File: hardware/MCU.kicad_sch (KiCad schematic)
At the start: 34 parts, among them J2 USB_C_Receptacle_USB2.0_16P, J3 Sensor, J4 Display, Q2 MMBT3904, Q3 MMBT3904, U2 CP2102-GM, U3 AKS1201, U4 ESP32-WROOM-32E-N4

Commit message: updated layout
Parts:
- added C22: 1u, Capacitor_SMD:C_0603_1608Metric, symbol Device:C_Small
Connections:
- net 3V3_MCU: now also C22.1
- net GND: now also C22.2
- net USB_CONN_D+: now reaches J2.A7 (D-), J2.B7 (D-), U3.1 (I/O1)
- net USB_CONN_D-: now reaches J2.A6 (D+), J2.B6 (D+), U3.3 (I/O2)
- net USB_DM renamed USB_D+
- net USB_D+: now also U2.4 (D+); no longer U2.5 (D-)
- net USB_DP renamed USB_D-
- net USB_D-: now also U2.5 (D-); no longer U2.4 (D+)
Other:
- moved on the sheet: R10, R11, R17, U3

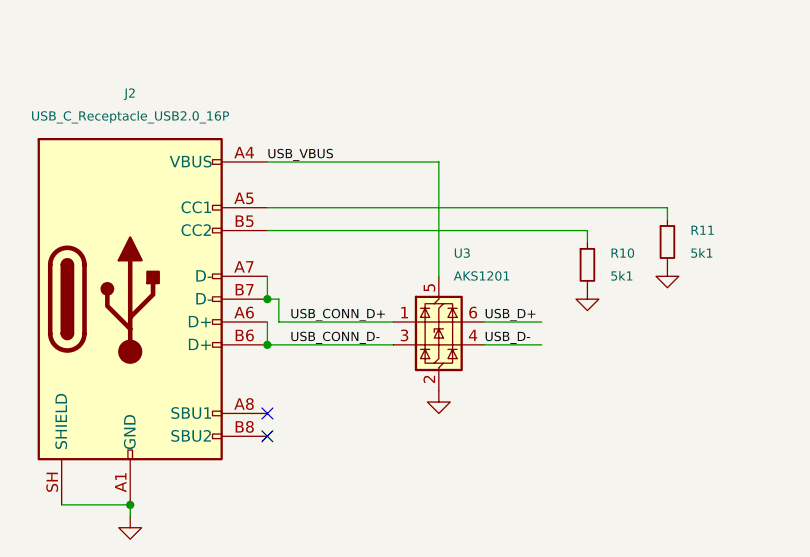
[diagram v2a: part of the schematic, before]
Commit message: updated layout
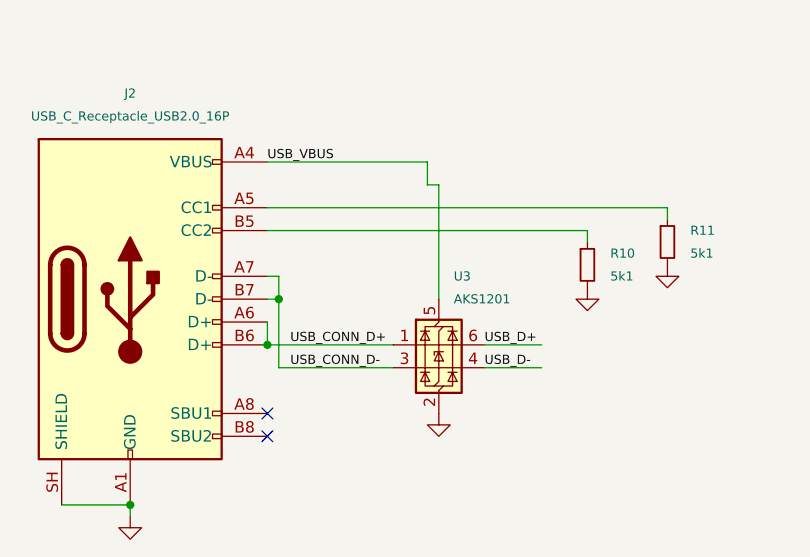
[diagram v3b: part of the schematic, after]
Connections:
- net USB_CONN_D+: now also J2.A6 (D+), J2.B6 (D+); no longer J2.A7 (D-), J2.B7 (D-)
- net USB_CONN_D-: now also J2.A7 (D-), J2.B7 (D-); no longer J2.A6 (D+), J2.B6 (D+)
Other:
- moved on the sheet: U3
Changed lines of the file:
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@@
 	)
 	(junction
+		(at 91.44 163.83)
+		(diameter 0)
+		(color 0 0 0 0)
+	)
+	(junction
 		(at 143.51 62.23)
 		(diameter 0)
@@
 	)
 	(junction
-		(at 90.17 168.91)
-		(diameter 0)
-		(color 0 0 0 0)
-	)
-	(junction
 		(at 228.6 100.33)
 		(diameter 0)
@@
 	)
 	(junction
-		(at 90.17 163.83)
+		(at 90.17 168.91)
 		(diameter 0)
 		(color 0 0 0 0)
@@
 	(wire
 		(pts
+			(xy 107.95 148.59) (xy 90.17 148.59)
+		)
+		(stroke
+			(width 0)
+			(type default)
+		)
+	)
+	(wire
+		(pts
 			(xy 90.17 45.72) (xy 90.17 46.99)
 		)
@@
 	(wire
 		(pts
-			(xy 114.3 168.91) (xy 120.65 168.91)
+			(xy 114.3 171.45) (xy 120.65 171.45)
 		)
 		(stroke
@@
 	(wire
 		(pts
-			(xy 109.22 161.29) (xy 109.22 148.59)
+			(xy 109.22 163.83) (xy 109.22 151.13)
 		)
 		(stroke
@@
 	(wire
 		(pts
-			(xy 90.17 161.29) (xy 90.17 163.83)
+			(xy 90.17 168.91) (xy 104.14 168.91)
 		)
 		(stroke
@@
 	(wire
 		(pts
-			(xy 91.44 163.83) (xy 90.17 163.83)
-		)
-		(stroke
-			(width 0)
-			(type default)
-		)
-	)
-	(wire
-		(pts
 			(xy 90.17 52.07) (xy 90.17 53.34)
 		)
@@
 	(wire
 		(pts
+			(xy 90.17 163.83) (xy 91.44 163.83)
+		)
+		(stroke
+			(width 0)
+			(type default)
+		)
+	)
+	(wire
+		(pts
 			(xy 251.46 96.52) (xy 251.46 97.79)
 		)
@@
 	(wire
 		(pts
+			(xy 91.44 171.45) (xy 104.14 171.45)
+		)
+		(stroke
+			(width 0)
+			(type default)
+		)
+	)
+	(wire
+		(pts
 			(xy 199.39 115.57) (xy 201.93 115.57)
 		)
@@
 	(wire
 		(pts
-			(xy 165.1 41.91) (xy 184.15 41.91)
+			(xy 90.17 161.29) (xy 91.44 161.29)
 		)
 		(stroke
@@
 	(wire
 		(pts
-			(xy 66.04 45.72) (xy 73.66 45.72)
+			(xy 165.1 41.91) (xy 184.15 41.91)
 		)
 		(stroke
@@
 	(wire
 		(pts
-			(xy 91.44 163.83) (xy 91.44 166.37)
+			(xy 66.04 45.72) (xy 73.66 45.72)
 		)
 		(stroke
@@
 	(wire
 		(pts
-			(xy 90.17 166.37) (xy 90.17 168.91)
+			(xy 80.01 45.72) (xy 80.01 46.99)
 		)
 		(stroke
@@
 	(wire
 		(pts
-			(xy 80.01 45.72) (xy 80.01 46.99)
+			(xy 205.74 49.53) (xy 205.74 41.91)
 		)
 		(stroke
@@
 	(wire
 		(pts
-			(xy 205.74 49.53) (xy 205.74 41.91)
+			(xy 248.92 114.3) (xy 248.92 102.87)
 		)
 		(stroke
@@
 	(wire
 		(pts
-			(xy 248.92 114.3) (xy 248.92 102.87)
+			(xy 217.17 102.87) (xy 238.76 102.87)
 		)
 		(stroke
@@
 	(wire
 		(pts
-			(xy 217.17 102.87) (xy 238.76 102.87)
+			(xy 91.44 161.29) (xy 91.44 163.83)
 		)
 		(stroke
@@
 	(wire
 		(pts
+			(xy 107.95 151.13) (xy 107.95 148.59)
+		)
+		(stroke
+			(width 0)
+			(type default)
+		)
+	)
+	(wire
+		(pts
 			(xy 175.26 48.26) (xy 175.26 49.53)
 		)
@@
 	(wire
 		(pts
-			(xy 90.17 148.59) (xy 109.22 148.59)
+			(xy 107.95 151.13) (xy 109.22 151.13)
 		)
 		(stroke
@@
 	(wire
 		(pts
-			(xy 114.3 166.37) (xy 120.65 166.37)
+			(xy 114.3 168.91) (xy 120.65 168.91)
 		)
 		(stroke
@@
 	(wire
 		(pts
-			(xy 91.44 166.37) (xy 104.14 166.37)
+			(xy 228.6 86.36) (xy 228.6 88.9)
 		)
 		(stroke
@@
 	(wire
 		(pts
-			(xy 228.6 86.36) (xy 228.6 88.9)
+			(xy 175.26 41.91) (xy 175.26 43.18)
 		)
 		(stroke
@@
 	(wire
 		(pts
-			(xy 175.26 41.91) (xy 175.26 43.18)
+			(xy 90.17 166.37) (xy 90.17 168.91)
 		)
 		(stroke
@@
 	(wire
 		(pts
+			(xy 91.44 163.83) (xy 91.44 171.45)
+		)
+		(stroke
+			(width 0)
+			(type default)
+		)
+	)
+	(wire
+		(pts
 			(xy 154.94 48.26) (xy 154.94 49.53)
 		)
@@
 	(wire
 		(pts
-			(xy 90.17 168.91) (xy 104.14 168.91)
-		)
-		(stroke
-			(width 0)
-			(type default)
-		)
-	)
-	(wire
-		(pts
 			(xy 199.39 100.33) (xy 228.6 100.33)
 		)
@@
 	)
 	(label "USB_CONN_D+"
-		(at 92.71 166.37 0)
+		(at 92.71 168.91 0)
 		(effects
 			(font
@@
 	)
 	(label "USB_D+"
-		(at 114.3 166.37 0)
+		(at 114.3 168.91 0)
 		(effects
 			(font
@@
 	)
 	(label "USB_D-"
-		(at 114.3 168.91 0)
+		(at 114.3 171.45 0)
 		(effects
 			(font
@@
 	)
 	(label "USB_CONN_D-"
-		(at 92.71 168.91 0)
+		(at 92.71 171.45 0)
 		(effects
 			(font
@@
 	(symbol
 		(lib_id "Power_Protection:USBLC6-2SC6")
-		(at 109.22 166.37 0)
+		(at 109.22 168.91 0)
 		(unit 1)
 		(body_style 1)
@@
 		(fields_autoplaced yes)
 		(property "Reference" "U3"
-			(at 110.8711 158.75 0)
+			(at 110.8711 161.29 0)
 			(show_name no)
 			(do_not_autoplace no)
@@
 		)
 		(property "Value" "AKS1201"
-			(at 110.8711 161.29 0)
+			(at 110.8711 163.83 0)
 			(show_name no)
 			(do_not_autoplace no)
@@
 		)
 		(property "Footprint" "Package_TO_SOT_SMD:SOT-23-6"
-			(at 110.49 172.72 0)
+			(at 110.49 175.26 0)
 			(hide yes)
 			(show_name no)
@@
 		)
 		(property "Datasheet" "https://www.st.com/resource/en/datasheet/usblc6-2.pdf"
-			(at 110.49 174.625 0)
+			(at 110.49 177.165 0)
 			(hide yes)
 			(show_name no)
@@
 		)
 		(property "Description" "Very low capacitance ESD protection diode, 2 data-line, SOT-23-6"
-			(at 109.22 166.37 0)
+			(at 109.22 168.91 0)
 			(hide yes)
 			(show_name no)
@@
 		)
 		(property "Function" "U4"
-			(at 109.22 166.37 0)
+			(at 109.22 168.91 0)
 			(hide yes)
 			(show_name no)
@@
 		)
 		(property "Dielectric" ""
-			(at 109.22 166.37 0)
+			(at 109.22 168.91 0)
 			(hide yes)
 			(show_name no)
@@
 		)
 		(property "Tolerance" ""
-			(at 109.22 166.37 0)
+			(at 109.22 168.91 0)
 			(hide yes)
 			(show_name no)
@@
 		)
 		(property "Voltage" ""
-			(at 109.22 166.37 0)
+			(at 109.22 168.91 0)
 			(hide yes)
 			(show_name no)
@@
 		)
 		(property "Power" ""
-			(at 109.22 166.37 0)
+			(at 109.22 168.91 0)
 			(hide yes)
 			(show_name no)
@@
 		)
 		(property "TCR" ""
-			(at 109.22 166.37 0)
+			(at 109.22 168.91 0)
 			(hide yes)
 			(show_name no)
@@
 		)
 		(property "MPN" "AKS1201"
-			(at 109.22 166.37 0)
+			(at 109.22 168.91 0)
 			(hide yes)
 			(show_name no)
@@
 		)
 		(property "Manufacturer" "AKYGA SEMI"
-			(at 109.22 166.37 0)
+			(at 109.22 168.91 0)
 			(hide yes)
 			(show_name no)
@@
 	(symbol
 		(lib_id "power:GND")
-		(at 109.22 173.99 0)
+		(at 109.22 176.53 0)
 		(unit 1)
 		(body_style 1)
@@
 		(fields_autoplaced yes)
 		(property "Reference" "#PWR019"
-			(at 109.22 180.34 0)
+			(at 109.22 182.88 0)
 			(hide yes)
 			(show_name no)
@@
 		)
 		(property "Value" "GND"
-			(at 109.22 179.07 0)
+			(at 109.22 181.61 0)
 			(hide yes)
 			(show_name no)
@@
 		)
 		(property "Footprint" ""
-			(at 109.22 173.99 0)
+			(at 109.22 176.53 0)
 			(hide yes)
 			(show_name no)
@@
 		)
 		(property "Datasheet" ""
-			(at 109.22 173.99 0)
+			(at 109.22 176.53 0)
 			(hide yes)
 			(show_name no)
@@
 		)
 		(property "Description" "Power symbol creates a global label with name \"GND\" , ground"
-			(at 109.22 173.99 0)
+			(at 109.22 176.53 0)
 			(hide yes)
 			(show_name no)
